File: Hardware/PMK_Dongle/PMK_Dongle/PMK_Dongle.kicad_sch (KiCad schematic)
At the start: 9 parts

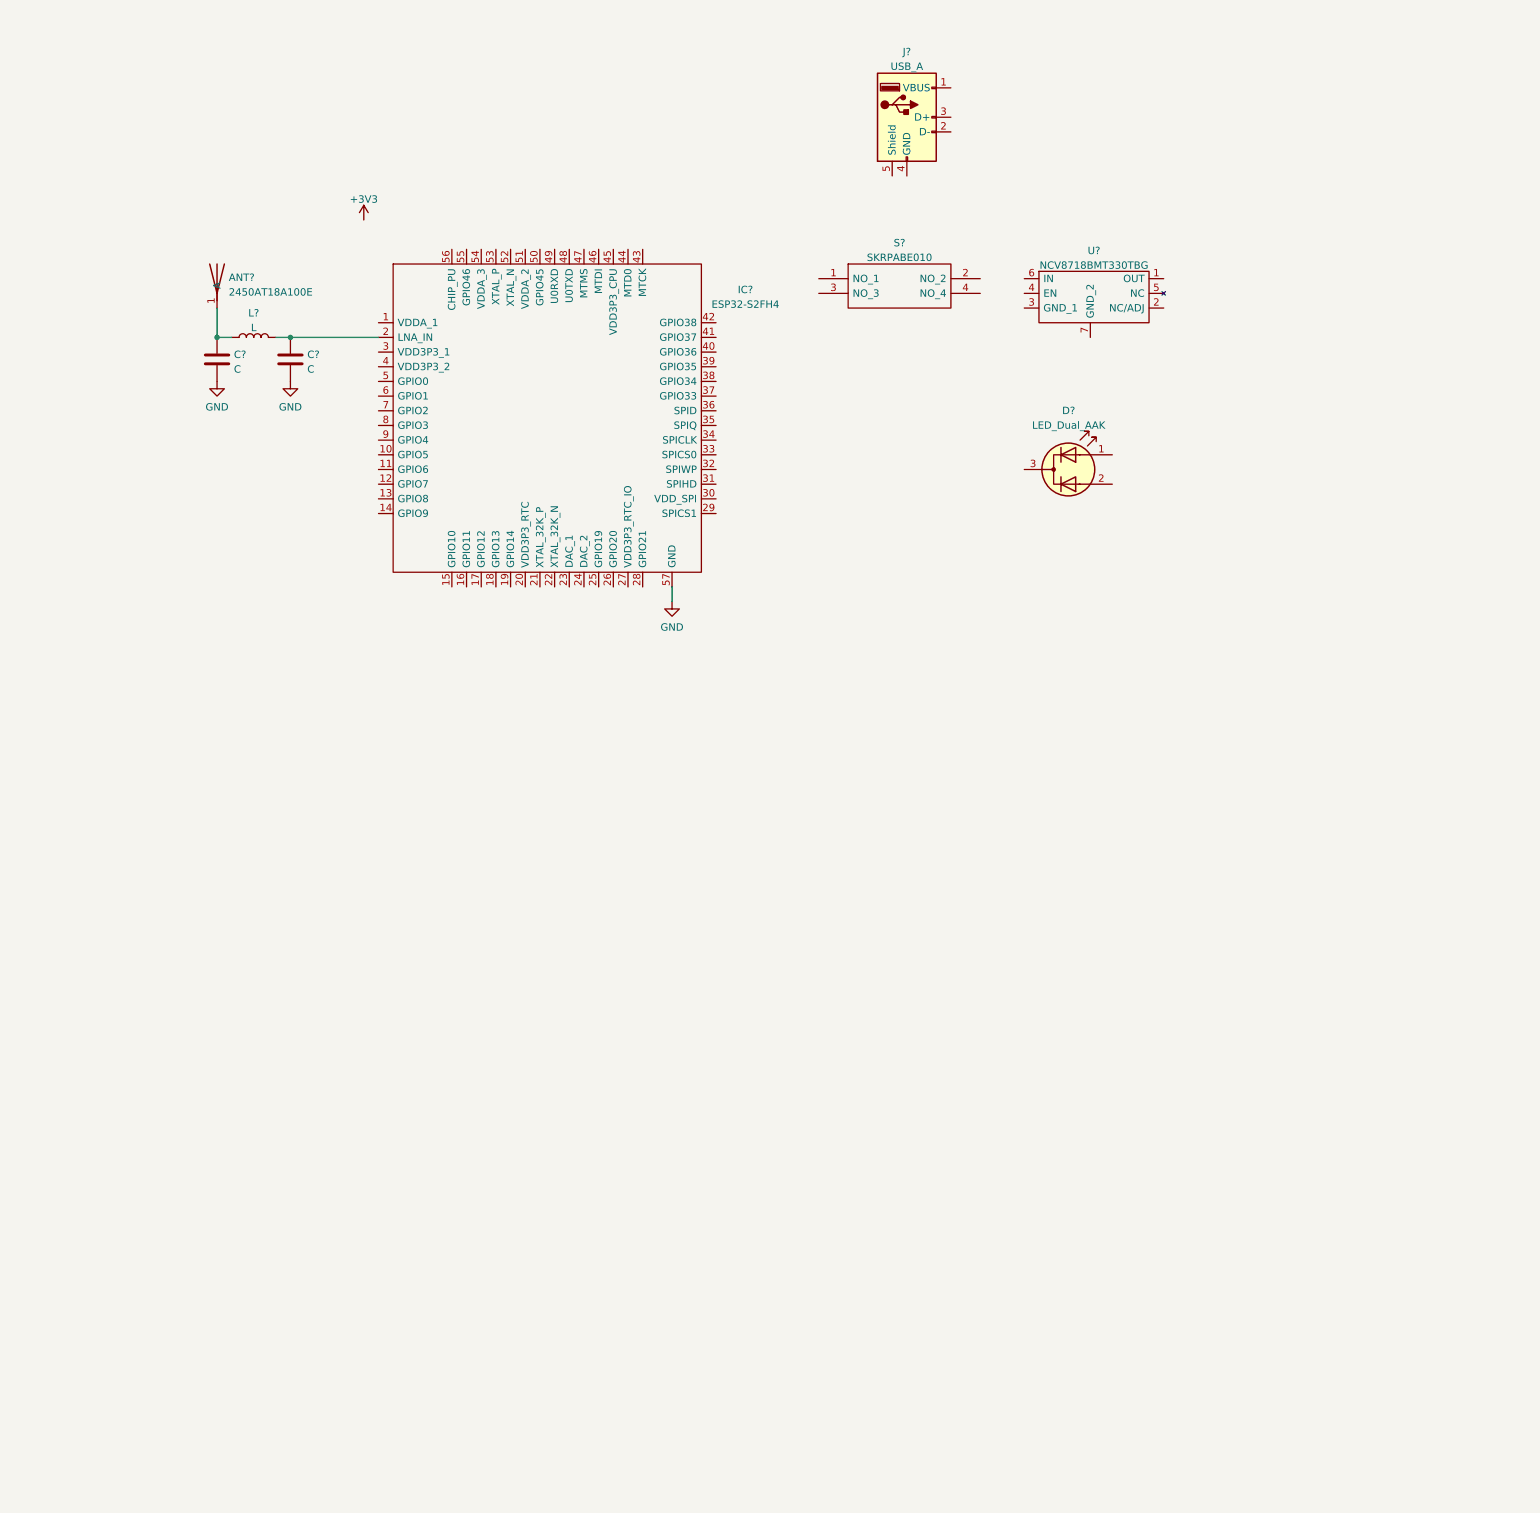
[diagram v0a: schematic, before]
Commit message: Added ESP32 to schematic
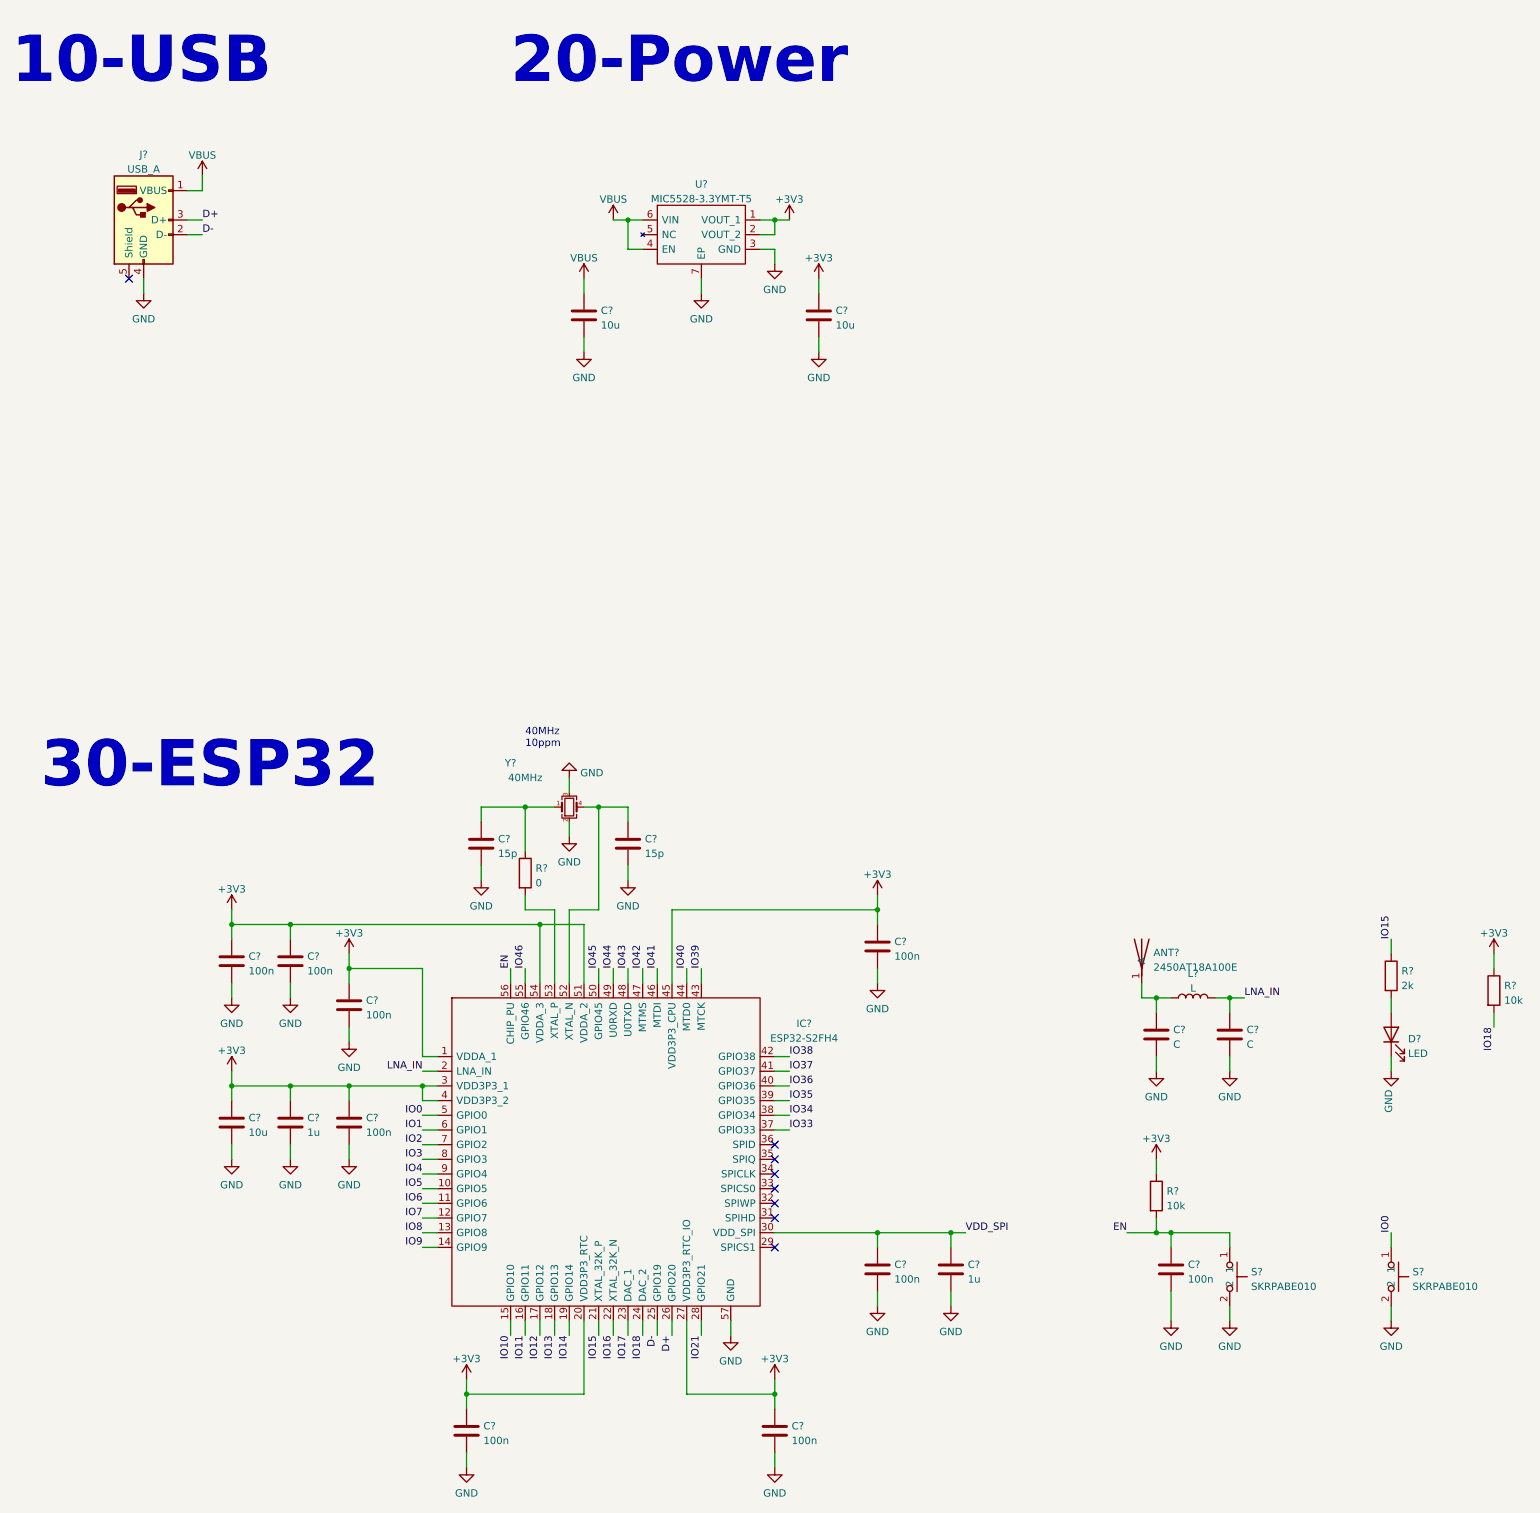
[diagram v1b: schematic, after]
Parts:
- removed ANT?: 2450AT18A100E, Component_lib:ANTC3216X140N, symbol Component_lib:2450AT18A100E
- removed C? (x2): C, Capacitor_SMD:C_0201_0603Metric, symbol Component_lib:C
- removed D?: LED_Dual_AAK, symbol Device:LED_Dual_AAK
- removed IC?: ESP32-S2FH4, QFN40P700X700X90-57N-D, symbol Component_lib:ESP32-S2FH4
- removed L?: L, Capacitor_SMD:C_0402_1005Metric, symbol Component_lib:L
- removed S?: SKRPABE010, SKRPABE010, symbol Component_lib_old:SKRPABE010
- removed U?: NCV8718BMT330TBG, SON65P200X200X80-7N, symbol Component_lib:NCV8718BMT330TBG
- added ANT?: 2450AT18A100E, ANTC3216X140N, symbol Component lib:2450AT18A100E
- added C? (x9): 100n, symbol Component lib:C
- added C? (x2): C, symbol Component lib:C
- added C? (x2): 1u, symbol Component lib:C
- added C? (x2): 15p, symbol Component lib:C
- added C? (x3): 10u, symbol Component lib:C
- added D?: LED, symbol Component lib:LED
- added IC?: ESP32-S2FH4, QFN40P700X700X90-57N-D, symbol Component lib:ESP32-S2FH4
- added L?: L, symbol Component lib:L
- added R? (x2): 10k, symbol Component lib:R
- added R?: 0, symbol Component lib:R
- added R?: 2k, symbol Component lib:R
- added S? (x2): SKRPABE010, SKRPABE010, symbol Component lib:SKRPABE010
- added U?: MIC5528-3.3YMT-T5, SON40P120X120X60-7N-D, symbol Component lib:MIC5528-3.3YMT-T5
- added Y?: 40MHz, symbol Device:Crystal_GND23_Small
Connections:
- net +3V3: now also C?.1, C?.1, C?.1, C?.1, C?.1, C?.1, C?.1, C?.1, C?.1, C?.1, IC?.1 (VDDA_1), IC?.20 (VDD3P3_RTC), IC?.27 (VDD3P3_RTC_IO), IC?.3 (VDD3P3_1), IC?.4 (VDD3P3_2), IC?.45 (VDD3P3_CPU), IC?.51 (VDDA_2), IC?.54 (VDDA_3), R?.1, R?.1, U?.1 (VOUT_1), U?.2 (VOUT_2)
- net GND: now also J?.4 (GND), C?.2, C?.2, C?.2, C?.2, C?.2, C?.2, C?.2, C?.2, C?.2, C?.2, C?.2, C?.2, C?.2, C?.2, C?.2, C?.2, C?.2, C?.2, D?.1 (K), IC?.57 (GND), S?.2, S?.2, U?.3 (GND), U?.7 (EP), Y?.2, Y?.3
- net VBUS: now reaches J?.1 (VBUS)
- net VBUS: now also C?.1, U?.4 (EN), U?.6 (VIN)
- net D-: now reaches J?.2 (D-)
- net D-: now also IC?.25 (GPIO19)
- net D+: now reaches J?.3 (D+)
- net D+: now also IC?.26 (GPIO20)
- new net: ANT?.1 (A), C?.1, L?.1
- new net: D?.2 (A), R?.2
- new net: C?.1, IC?.52 (XTAL_N), Y?.4
- new net: C?.1, R?.1, Y?.1
- new net: IC?.53 (XTAL_P), R?.2
- new net EN: C?.1, IC?.56 (CHIP_PU), R?.2, S?.1
- new net IO0: IC?.5 (GPIO0), S?.1
- new net IO1: IC?.6 (GPIO1)
- new net IO10: IC?.15 (GPIO10)
- new net IO11: IC?.16 (GPIO11)
- new net IO12: IC?.17 (GPIO12)
- new net IO13: IC?.18 (GPIO13)
- new net IO14: IC?.19 (GPIO14)
- new net IO15: IC?.21 (XTAL_32K_P), R?.1
- new net IO16: IC?.22 (XTAL_32K_N)
- new net IO17: IC?.23 (DAC_1)
- new net IO18: IC?.24 (DAC_2), R?.2
- new net IO2: IC?.7 (GPIO2)
- new net IO21: IC?.28 (GPIO21)
- new net IO3: IC?.8 (GPIO3)
- new net IO33: IC?.37 (GPIO33)
- new net IO34: IC?.38 (GPIO34)
- new net IO35: IC?.39 (GPIO35)
- new net IO36: IC?.40 (GPIO36)
- new net IO37: IC?.41 (GPIO37)
- new net IO38: IC?.42 (GPIO38)
- new net IO39: IC?.43 (MTCK)
- new net IO4: IC?.9 (GPIO4)
- new net IO40: IC?.44 (MTD0)
- new net IO41: IC?.46 (MTDI)
- new net IO42: IC?.47 (MTMS)
- new net IO43: IC?.48 (U0TXD)
- new net IO44: IC?.49 (U0RXD)
- new net IO45: IC?.50 (GPIO45)
- new net IO46: IC?.55 (GPIO46)
- new net IO5: IC?.10 (GPIO5)
- new net IO6: IC?.11 (GPIO6)
- new net IO7: IC?.12 (GPIO7)
- new net IO8: IC?.13 (GPIO8)
- new net IO9: IC?.14 (GPIO9)
- new net LNA_IN: C?.1, IC?.2 (LNA_IN), L?.2
- new net VDD_SPI: C?.1, C?.1, IC?.30 (VDD_SPI)
- no-connect marks 0 -> 8
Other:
- note added: "10-USB"
- note added: "20-Power"
- note added: "30-ESP32"
- note added: "40MHz 10ppm"
- company: (none) -> Puma Corp
- title: (none) -> PMK_Dongle
- moved on the sheet: J?

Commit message: Started routing
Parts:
- ANT1: renamed from ANT?; footprint ANTC3216X140N -> Component_lib:ANTC3216X140N
- C1, C11, C2: renamed from C?; footprint (none) -> Capacitor_SMD:C_0603_1608Metric
- C10, C3, C4, C9: renamed from C?; footprint (none) -> Capacitor_SMD:C_0201_0603Metric
- C12, C13, C14, C15, C16, C17, C18, C5, C6, C7, C8: renamed from C?; footprint (none) -> Capacitor_SMD:C_0402_1005Metric
- D1: renamed from D?; footprint (none) -> Capacitor_SMD:C_0402_1005Metric
- IC1: renamed from IC?; footprint QFN40P700X700X90-57N-D -> Component_lib:QFN40P700X700X90-57N-D
- J1: renamed from J?; footprint (none) -> Component_lib:USB_PCB
- L1: renamed from L?; footprint (none) -> Capacitor_SMD:C_0201_0603Metric
- R1, R3, R4: renamed from R?; footprint (none) -> Capacitor_SMD:C_0201_0603Metric
- R2: renamed from R?; footprint (none) -> Capacitor_SMD:C_0402_1005Metric
- S1, S2: renamed from S?; footprint SKRPABE010 -> Component_lib:SKRPABE010
- U1: renamed from U?; footprint SON40P120X120X60-7N-D -> Component_lib:SON40P120X120X60-7N-D
- Y1: renamed from Y?; footprint (none) -> Component_lib:NX2016SA32MEXS00ACS06465
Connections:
- net QUARTZ_2: now reaches C4.1, IC1.52 (XTAL_N), Y1.4
- net QUARTZ_1: now reaches C3.1, R1.1, Y1.1
- net QUARTZ_3: now reaches IC1.53 (XTAL_P), R1.2

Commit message: Layout is almost done
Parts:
- D1: footprint Capacitor_SMD:C_0402_1005Metric -> LED_SMD:LED_0402_1005Metric
- L1: footprint Capacitor_SMD:C_0201_0603Metric -> Inductor_SMD:L_0201_0603Metric
- R1, R3: footprint Capacitor_SMD:C_0201_0603Metric -> Resistor_SMD:R_0201_0603Metric
- R2: footprint Capacitor_SMD:C_0402_1005Metric -> Resistor_SMD:R_0402_1005Metric
- R4: footprint Capacitor_SMD:C_0201_0603Metric -> Resistor_SMD:R_0402_1005Metric
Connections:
- net IO15: no longer R2.1
- net IO46: now also R2.1
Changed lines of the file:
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@@
     (effects (font (size 1.27 1.27)) (justify left bottom))
   )
-  (label "IO15" (at 254 180.34 90)
+  (label "IO46" (at 254 180.34 90)
     (effects (font (size 1.27 1.27)) (justify left bottom))
   )
@@
     (property "Reference" "L1" (id 0) (at 219.71 186.2922 0))
     (property "Value" "L" (id 1) (at 219.71 188.8291 0))
-    (property "Footprint" "Capacitor_SMD:C_0201_0603Metric" (id 2) (at 219.71 190.5 90)
+    (property "Footprint" "Inductor_SMD:L_0201_0603Metric" (id 2) (at 219.71 190.5 90)
       (effects (font (size 1.27 1.27)) hide)
     )
@@
       (effects (font (size 1.27 1.27)) (justify left))
     )
-    (property "Footprint" "Capacitor_SMD:C_0201_0603Metric" (id 2) (at 211.582 224.79 90)
+    (property "Footprint" "Resistor_SMD:R_0402_1005Metric" (id 2) (at 211.582 224.79 90)
       (effects (font (size 1.27 1.27)) hide)
     )
@@
       (effects (font (size 1.27 1.27)) (justify left))
     )
-    (property "Footprint" "Capacitor_SMD:C_0201_0603Metric" (id 2) (at 270.002 189.23 90)
+    (property "Footprint" "Resistor_SMD:R_0201_0603Metric" (id 2) (at 270.002 189.23 90)
       (effects (font (size 1.27 1.27)) hide)
     )
@@
       (effects (font (size 1.27 1.27)) (justify right))
     )
-    (property "Footprint" "Capacitor_SMD:C_0402_1005Metric" (id 2) (at 254 196.85 0)
+    (property "Footprint" "LED_SMD:LED_0402_1005Metric" (id 2) (at 254 196.85 0)
       (effects (font (size 1.27 1.27)) hide)
     )
@@
       (effects (font (size 1.27 1.27)) (justify left))
     )
-    (property "Footprint" "Capacitor_SMD:C_0201_0603Metric" (id 2) (at 102.362 168.91 90)
+    (property "Footprint" "Resistor_SMD:R_0201_0603Metric" (id 2) (at 102.362 168.91 90)
       (effects (font (size 1.27 1.27)) hide)
     )
@@
       (effects (font (size 1.27 1.27)) (justify left))
     )
-    (property "Footprint" "Capacitor_SMD:C_0402_1005Metric" (id 2) (at 252.222 186.69 90)
+    (property "Footprint" "Resistor_SMD:R_0402_1005Metric" (id 2) (at 252.222 186.69 90)
       (effects (font (size 1.27 1.27)) hide)
     )
@@
     )
     (path "/99144121-f245-4dd2-9fa9-a5205ddd114c"
-      (reference "D1") (unit 1) (value "LED") (footprint "Capacitor_SMD:C_0402_1005Metric")
+      (reference "D1") (unit 1) (value "LED") (footprint "LED_SMD:LED_0402_1005Metric")
     )
     (path "/c050aa66-7824-4881-8613-3d9bc922e5ba"
@@
     )
     (path "/440df312-390c-4905-a0d0-730c7e7600cf"
-      (reference "L1") (unit 1) (value "L") (footprint "Capacitor_SMD:C_0201_0603Metric")
+      (reference "L1") (unit 1) (value "L") (footprint "Inductor_SMD:L_0201_0603Metric")
     )
     (path "/a7b61a5a-cac0-44ec-bc4d-33c9657318e5"
-      (reference "R1") (unit 1) (value "0") (footprint "Capacitor_SMD:C_0201_0603Metric")
+      (reference "R1") (unit 1) (value "0") (footprint "Resistor_SMD:R_0201_0603Metric")
     )
     (path "/cb8cd454-dc1e-4302-8d06-bab6cf314635"
-      (reference "R2") (unit 1) (value "2k") (footprint "Capacitor_SMD:C_0402_1005Metric")
+      (reference "R2") (unit 1) (value "2k") (footprint "Resistor_SMD:R_0402_1005Metric")
     )
     (path "/5eb3170b-1d89-433f-97fe-7659b94468c4"
-      (reference "R3") (unit 1) (value "10k") (footprint "Capacitor_SMD:C_0201_0603Metric")
+      (reference "R3") (unit 1) (value "10k") (footprint "Resistor_SMD:R_0201_0603Metric")
     )
     (path "/49ec081a-adad-4714-8be8-a2fd00fa5acd"
-      (reference "R4") (unit 1) (value "10k") (footprint "Capacitor_SMD:C_0201_0603Metric")
+      (reference "R4") (unit 1) (value "10k") (footprint "Resistor_SMD:R_0402_1005Metric")
     )
     (path "/60762a72-d9b3-4954-9033-a13f26ad9b62"
